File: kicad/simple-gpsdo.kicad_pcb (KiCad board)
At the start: 2 copper layers, 119.5 x 74.5 mm, 102 parts, among them J1 PPS_OUT, J2 PWR, J3 ISP, J4 GPS_NEO, J5 GPS_IN, J6 10MHz_OUT, J7 NEO-6M, J8 10MHz_OUT, J9 USB_C, Q1 DMP3099L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

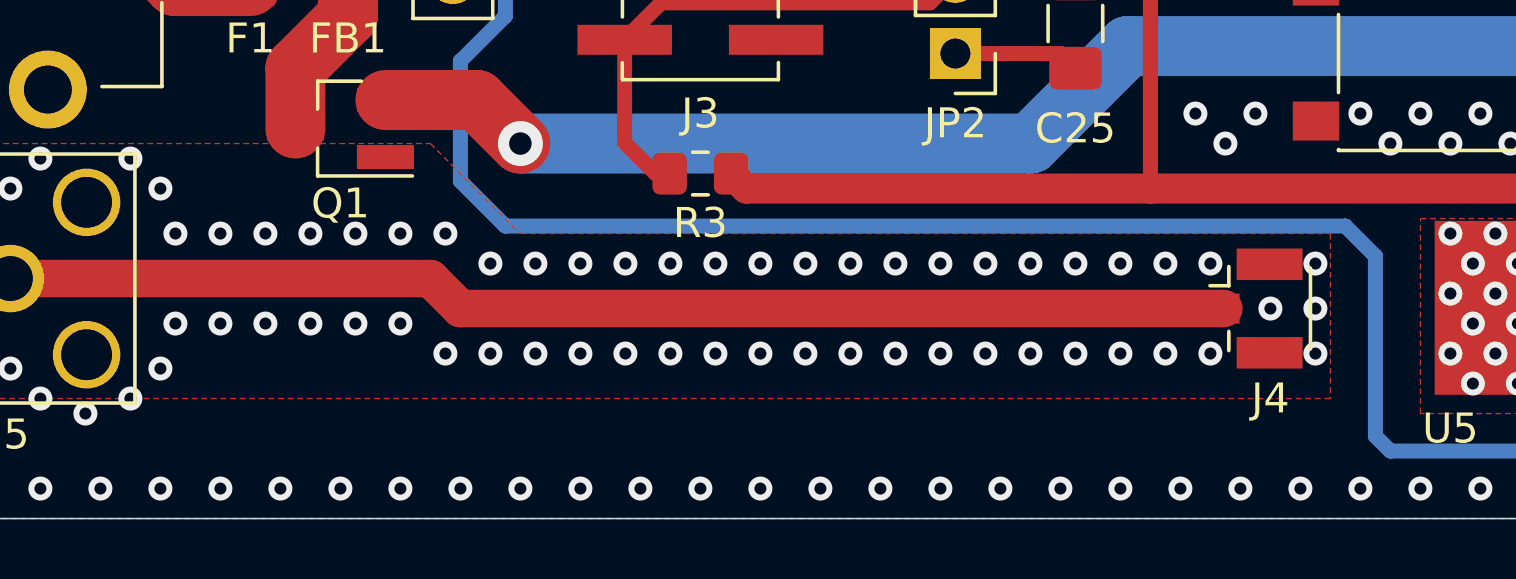
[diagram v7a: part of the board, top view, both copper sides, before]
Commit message: updated board with silkscreen logo and text
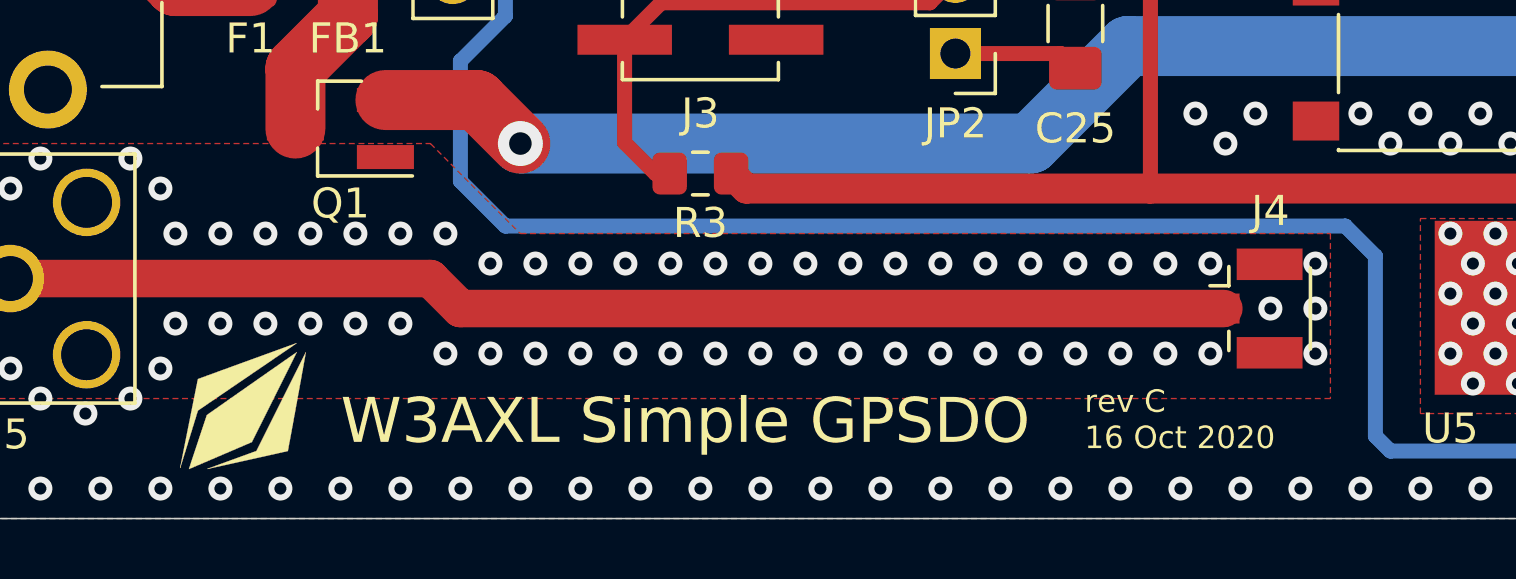
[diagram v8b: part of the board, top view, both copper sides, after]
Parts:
- added G***: LOGO, w3axl-logos:logo-4.2x4.2, F.Cu at (88.8, 145.8)
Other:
- board text added: "W3AXL Simple GPSDO"
- board text added: "rev C 16 Oct 2020"
